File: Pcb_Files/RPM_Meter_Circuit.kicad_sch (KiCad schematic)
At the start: 22 parts, among them J1 5V INPUT, M1 Motor_DC, Q1 2N3904, Q2 2N3904, Q3 IRF540N, SW1 SW_Push, U1 PIC18F26J50-I_SP, U2 AMS1117-3.3, U3 ST7735_128_x_160

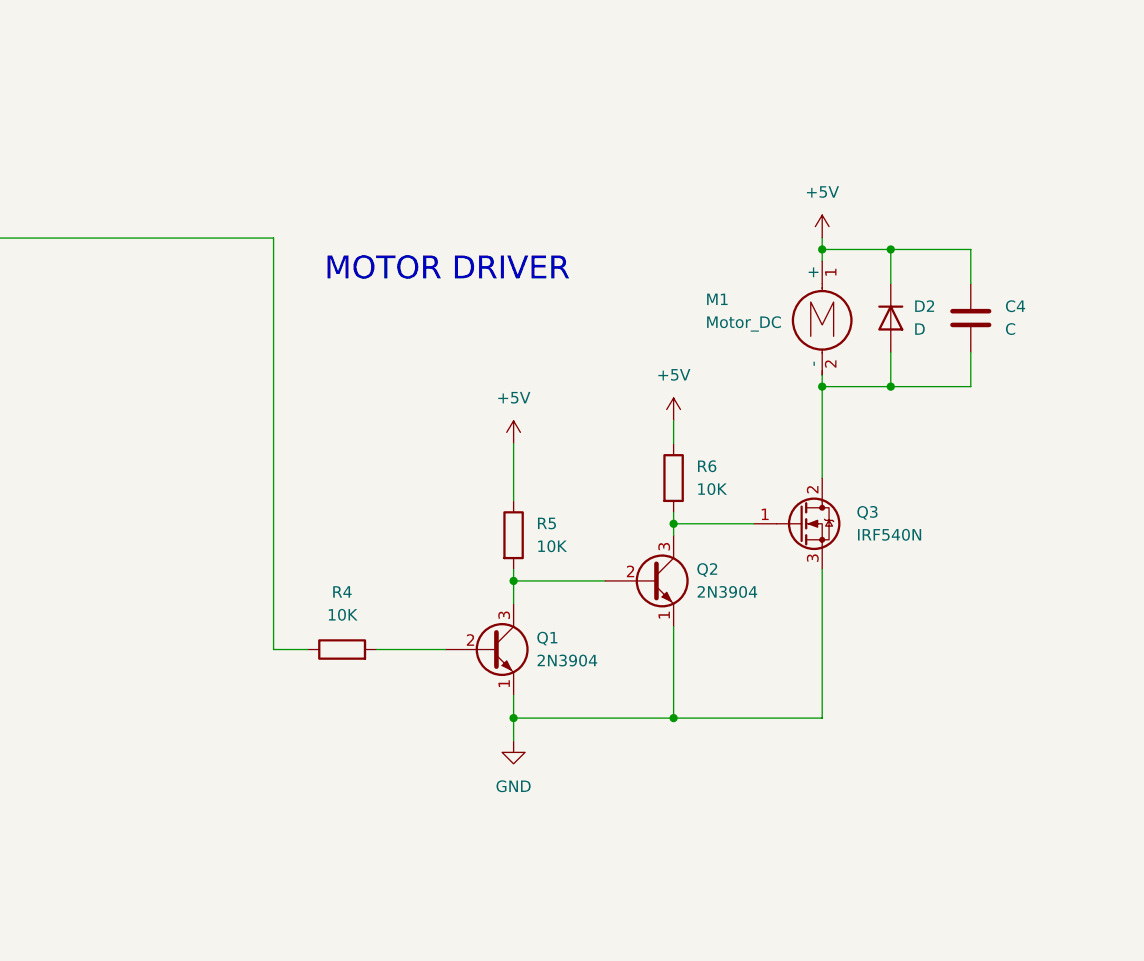
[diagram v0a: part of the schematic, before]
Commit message: Feat : Updated Schematic Kicad Circuit, Added Function for PWM control.
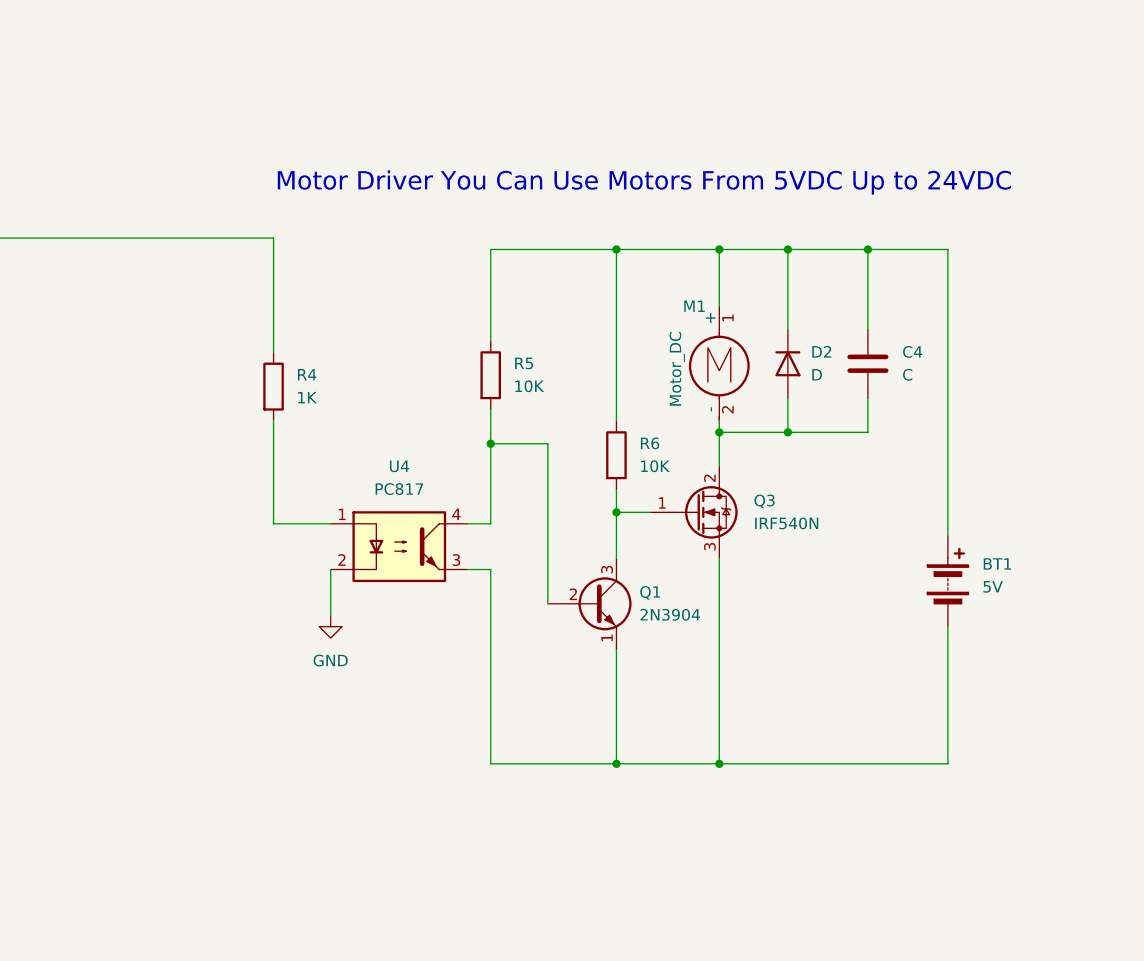
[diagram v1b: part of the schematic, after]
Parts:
- removed Q2: 2N3904, Package_TO_SOT_THT:TO-92_Inline, symbol Transistor_BJT:2N3904
- added BT1: 5V, symbol Device:Battery
- added U4: PC817, Package_DIP:DIP-4_W7.62mm, symbol Isolator:PC817
- R4: value 10K -> 1K
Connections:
- net +5V: no longer C4.1, D2.1 (K), M1.1 (+), R5.1, R6.1
- net GND: now also U4.2; no longer Q1.1 (E), Q3.3 (S)
- net at Q3.1 (G), R6.2: now also Q1.3 (C)
- net at R5.2: now also Q1.2 (B), U4.4; no longer Q1.3 (C)
- net at R4.2: now also U4.1; no longer Q1.2 (B)
- new net: BT1.2 (-), Q1.1 (E), Q3.3 (S), U4.3
- new net: BT1.1 (+), C4.1, D2.1 (K), M1.1 (+), R5.1, R6.1
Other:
- note added: "Motor Driver You Can Use Motors From 5VDC Up to 24VDC"
- note removed: "MOTOR DRIVER"
- moved on the sheet: C4, D2, M1, Q3
